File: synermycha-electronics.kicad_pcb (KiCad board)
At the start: 4 copper layers, 128 x 124.5 mm, 114 parts, among them J10 Conn_01x04, J11 USB_B_Micro, J2 Conn_01x02, J3 Conn_01x02, J4 USB_B_Micro, J5 ESP_01, J6 Conn_01x04, J7 Conn_01x04, J8 Conn_01x04, J9 Conn_01x04, Q1 IRLML9301TRPBF, Q2 Q_NPN_EBC, Q3 Q_NPN_EBC, Q4 BC847, SW1 DTSM32N, SW2 DTSM32N, SW3 DTSM32N, SW4 DTSM32N, SW5 SW_SPDT, U1 LM1117LDX, U10 AS5045B, U11 AS5045B, U12 MPU-9250, U13 STM32F446RETx, U14 STM14_SW, U2 LM1117LDX, U3 LM1117LDX, U4 DRV8835, U5 VL53L0X, U6 VL53L0X, U7 VL53L0X, U8 CP2102N-A01-GQFN28, U9 TS5A3167DBVR, Y1 16MHz, 8pF

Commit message: Major upgrade
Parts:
- removed R11, R12, R13: 47K, Resistor_SMD:R_0402_1005Metric
- removed SW5: SW_SPDT, Connector_PinHeader_2.54mm:PinHeader_2x03_P2.54mm_Vertical_SMD
- removed U5, U6, U7: VL53L0X, synermycha-electronics:SENSOR_VL53L0X
- added J1: BATT, Connector_PinHeader_2.54mm:PinHeader_1x02_P2.54mm_Vertical, F.Cu at (38.5, 188.0)
- added J12: Conn_01x05, connector_brd2brd:01x05_1.0x0.5mm_SMD, F.Cu at (37.0, 126.0)
- added J13: Conn_01x05, connector_brd2brd:01x05_1.0x0.5mm_SMD, F.Cu at (59.0, 148.0)
- added J14: Conn_01x05, connector_brd2brd:01x05_1.0x0.5mm_SMD, F.Cu at (15.0, 148.0)
- added J15: Conn_01x05, connector_brd2brd:01x05_1.0x0.5mm_SMD, F.Cu at (21.3, 133.3)
- added J16: Conn_01x05, connector_brd2brd:01x05_1.0x0.5mm_SMD, F.Cu at (52.7, 133.3)
- added J17: Conn_01x03, Button_Switch_SMD:SW_SPDT_CK-JS102011SAQN, F.Cu at (37.0, 194.0)
- BZ1: value SMT-0825-T-2 -> CMT-5023S
- D10, D11, D12, D13, D7, D8, D9: footprint LED_SMD:LED_WS2812B_PLCC4_5.0x5.0mm_P3.2mm -> WS2812-2020:WS28122020
- R21: footprint Resistor_SMD:R_0805_2012Metric -> Resistor_SMD:R_0402_1005Metric
- moved C10 77.4 mm to (88.0, 165.5)
- moved R7 77.4 mm to (89.2, 165.5)
- moved R26 43.5 mm to (28.8, 145.8), turned to 0 degrees
- moved C12 39.8 mm to (91.0, 176.0)
- moved R9 38.0 mm to (91.0, 178.0)
- moved R8 30.0 mm to (80.0, 172.0)
- moved C11 29.8 mm to (80.0, 174.0)
- moved D6 29.3 mm to (24.2, 144.8)
- moved G*** 29.3 mm to (22.0, 147.0)
- moved U14 28.1 mm to (48.0, 144.0), turned to 180 degrees
- moved C21 26.2 mm to (-66.0, 201.7)
- moved C22 26.2 mm to (-66.6, 203.9)
- moved C23 26.2 mm to (-63.6, 203.9)
- moved C20 26.2 mm to (-63.4, 199.2)
- moved J10 26.2 mm to (-70.8, 202.9)
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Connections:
- J7 pad 3: (no net) -> /Encoders/ENC_L_A
- J7 pad 4: (no net) -> /Encoders/ENC_L_B
- J8 pad 3: (no net) -> /Encoders/ENC_R_A
- J8 pad 4: (no net) -> /Encoders/ENC_R_B
- U12 pad 23: (no net) -> /IMU/IMU_SCL
- U12 pad 24: (no net) -> /IMU/IMU_SDA
- U13 pad 16: (no net) -> /WiFi/ESP_RX
- U13 pad 17: (no net) -> /WiFi/ESP_TX
- U13 pad 22: (no net) -> /Encoders/ENC_R_A
- U13 pad 23: (no net) -> /Encoders/ENC_R_B
- U13 pad 33: (no net) -> /Motors & Motors Drivers/DRV8835_EN
- U13 pad 34: (no net) -> /Motors & Motors Drivers/DRV8835_DIR_A
- U13 pad 35: (no net) -> /Motors & Motors Drivers/DRV8835_PWM_A
- U13 pad 36: (no net) -> /Motors & Motors Drivers/DRV8835_PWM_B
- U13 pad 37: (no net) -> /Motors & Motors Drivers/DRV8835_DIR_B
- U13 pad 40: (no net) -> /IMU/IMU_SDA
- U13 pad 41: (no net) -> /IMU/IMU_SCL
- U13 pad 49: (no net) -> /uController/SWDCLK
- U13 pad 55: (no net) -> /uController/SWDO
- U13 pad 58: (no net) -> /Encoders/ENC_L_B
- U13 pad 59: (no net) -> /Encoders/ENC_L_A
- U13 pad 61: (no net) -> /Distance Sensors/VL53L0x_SCL
- U13 pad 62: (no net) -> /Distance Sensors/VL53L0x_SDA
- U14 pad 6: GND -> /uController/SWDCLK
- U14 pad 8: (no net) -> /uController/SWDO
- U4 pad 10: (no net) -> /Motors & Motors Drivers/DRV8835_DIR_A
- U4 pad 11: (no net) -> /Motors & Motors Drivers/DRV8835_EN
- U4 pad 7: (no net) -> /Motors & Motors Drivers/DRV8835_PWM_B
- U4 pad 8: (no net) -> /Motors & Motors Drivers/DRV8835_DIR_B
- U4 pad 9: (no net) -> /Motors & Motors Drivers/DRV8835_PWM_A
- U9 pad 1: (no net) -> /WiFi/ESP_RX
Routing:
- net +2V8: track 18.4 -> 140.6 mm, vias 3 -> 0
- net /Distance Sensors/VL53L0x_SDA: track 0.00 -> 96.4 mm, vias 0 -> 6
- net /Distance Sensors/VL53L0x_SCL: track 0.00 -> 88.3 mm, vias 0 -> 6
- net /uController/STM32_D+: track 0.00 -> 55.3 mm, vias 0 -> 2
- net /uController/STM32_D-: track 0.00 -> 55.3 mm, vias 0 -> 2
- net +6V: track 0.00 -> 42.8 mm
- net +3V3: track 65.8 -> 107.6 mm
- net /Motors & Motors Drivers/DRV8835_PWM_B: track 0.00 -> 21.9 mm, vias 0 -> 2
- net /Motors & Motors Drivers/DRV8835_DIR_B: track 0.00 -> 20.8 mm
- net /Motors & Motors Drivers/DRV8835_PWM_A: track 0.00 -> 20.6 mm
- net /Motors & Motors Drivers/DRV8835_DIR_A: track 0.00 -> 20.2 mm
- net /Motors & Motors Drivers/DRV8835_EN: track 0.00 -> 20.2 mm
- net Net-(Q2-Pad2): track 0.00 -> 16.8 mm
- net /WiFi/ESP_VBUS: track 5.61 -> 18.0 mm
- net /uController/SWDIO: track 0.00 -> 8.93 mm
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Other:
- board size 128 x 124.5 mm -> 50 x 75 mm
- board text added: "+"
- board text added: "-"
- board text added: "2C 7.4V"

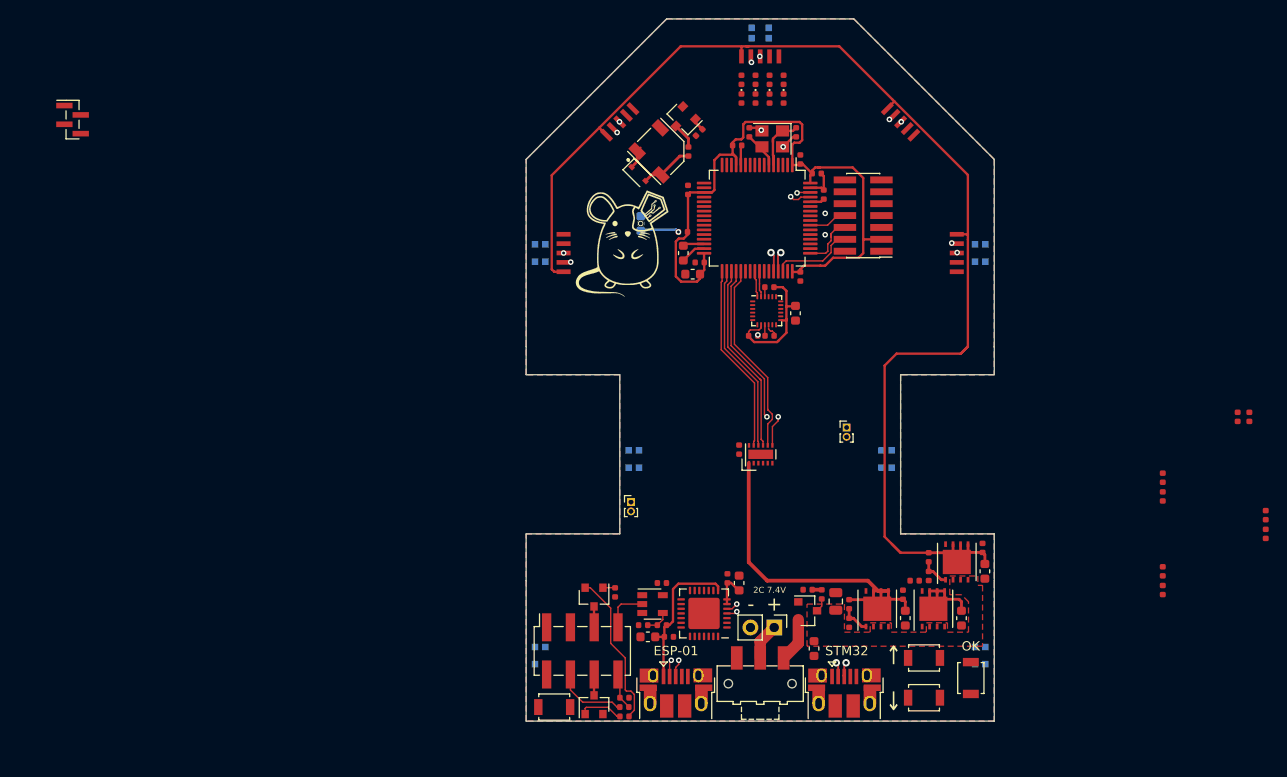
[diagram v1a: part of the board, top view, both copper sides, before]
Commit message: Many updates
Added 3V3<->2V8 conversion for VC53L0x and leds for XSHUT of those. PCB update
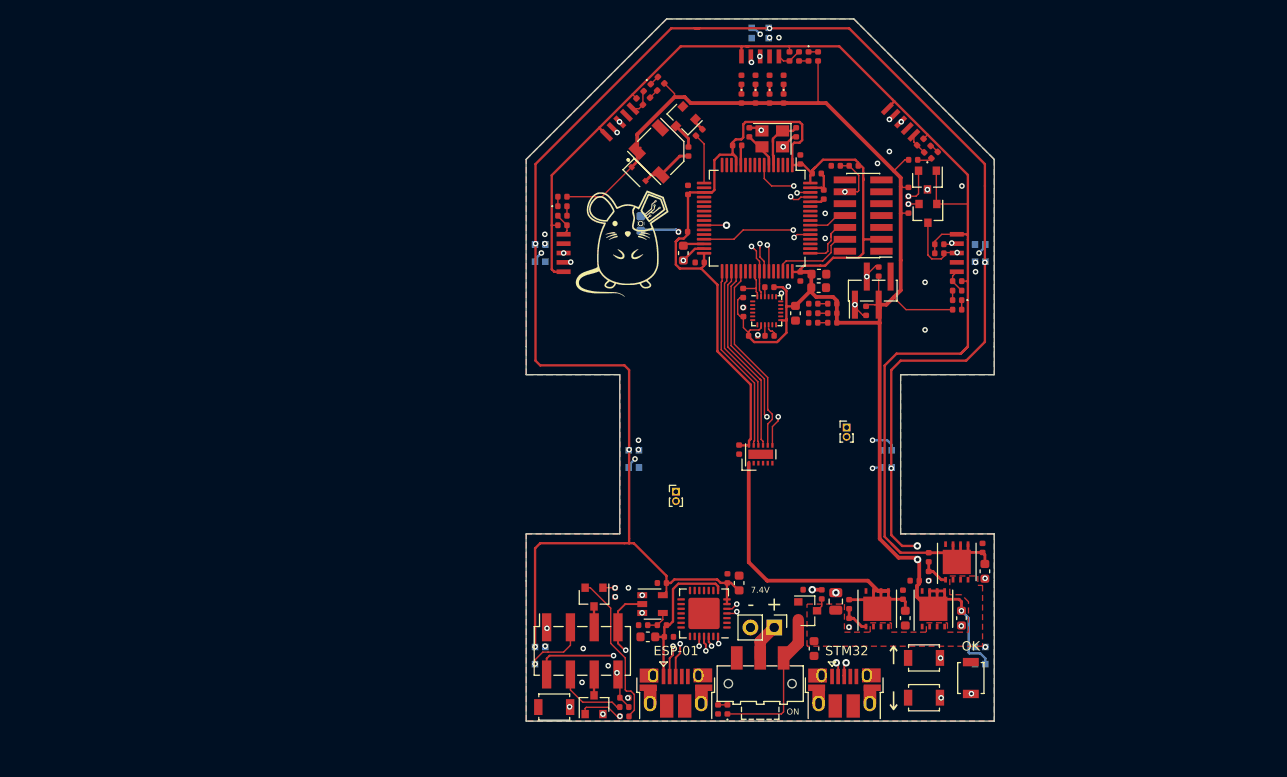
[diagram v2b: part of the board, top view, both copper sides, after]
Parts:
- added C37: 10uF, Capacitor_SMD:C_0603_1608Metric, F.Cu at (43.2, 151.7)
- added D14: RED, LED_SMD:LED_0402_1005Metric, F.Cu at (33.5, 196.8)
- added D15: YELLOW, LED_SMD:LED_0402_1005Metric, F.Cu at (42.2, 127.0)
- added D16: YELLOW, LED_SMD:LED_0402_1005Metric, F.Cu at (58.0, 153.0)
- added D17: YELLOW, LED_SMD:LED_0402_1005Metric, F.Cu at (15.9, 143.0)
- added D18: YELLOW, LED_SMD:LED_0402_1005Metric, F.Cu at (25.7, 130.3)
- added D19: YELLOW, LED_SMD:LED_0402_1005Metric, F.Cu at (55.6, 137.5)
- added Q5: Q_NMOS_GDS, Package_TO_SOT_SMD:SOT-23, F.Cu at (54.9, 140.2)
- added Q6: Q_NMOS_GDS, Package_TO_SOT_SMD:SOT-23, F.Cu at (54.9, 143.8)
- added R11: 2K2, Resistor_SMD:R_0402_1005Metric, F.Cu at (48.3, 154.2)
- added R12: 2K2, Resistor_SMD:R_0402_1005Metric, F.Cu at (35.2, 152.3)
- added R13: 2K2, Resistor_SMD:R_0402_1005Metric, F.Cu at (35.2, 154.3)
- added R30: 2K2, Resistor_SMD:R_0402_1005Metric, F.Cu at (49.7, 150.0)
- added R31: 2K2, Resistor_SMD:R_0402_1005Metric, F.Cu at (52.8, 143.3)
- added R32: 2K2, Resistor_SMD:R_0402_1005Metric, F.Cu at (52.8, 141.5)
- added R33: calculate, Resistor_SMD:R_0402_1005Metric, F.Cu at (32.5, 196.8)
- added R34: 2K2, Resistor_SMD:R_0402_1005Metric, F.Cu at (56.1, 148.0)
- added R35: 2K2, Resistor_SMD:R_0402_1005Metric, F.Cu at (56.1, 147.1)
- added R36: 1K, Resistor_SMD:R_0402_1005Metric, F.Cu at (41.1, 127.0)
- added R37: 1K, Resistor_SMD:R_0402_1005Metric, F.Cu at (58.0, 152.0)
- added R38: 1K, Resistor_SMD:R_0402_1005Metric, F.Cu at (15.9, 144.0)
- added R39: 1K, Resistor_SMD:R_0402_1005Metric, F.Cu at (24.9, 131.1)
- added R40: 1K, Resistor_SMD:R_0402_1005Metric, F.Cu at (54.9, 136.9)
- added R41: 47K, Resistor_SMD:R_0402_1005Metric, F.Cu at (40.1, 127.0)
- added R42: 47K, Resistor_SMD:R_0402_1005Metric, F.Cu at (58.0, 151.0)
- added R43: 47K, Resistor_SMD:R_0402_1005Metric, F.Cu at (15.9, 145.0)
- added R44: 47K, Resistor_SMD:R_0402_1005Metric, F.Cu at (24.1, 131.8)
- added R45: 47K, Resistor_SMD:R_0402_1005Metric, F.Cu at (54.1, 136.1)
- added R46: 1K, Resistor_SMD:R_0402_1005Metric, F.Cu at (43.2, 127.0)
- added R47: 1K, Resistor_SMD:R_0402_1005Metric, F.Cu at (58.0, 154.1)
- added R48: 1K, Resistor_SMD:R_0402_1005Metric, F.Cu at (15.9, 142.0)
- added R49: 1K, Resistor_SMD:R_0402_1005Metric, F.Cu at (26.4, 129.5)
- added R50: 1K, Resistor_SMD:R_0402_1005Metric, F.Cu at (53.3, 138.0)
- J6: footprint Connector_PinHeader_1.00mm:PinHeader_1x04_P1.00mm_Vertical_SMD_Pin1Left -> Connector_PinHeader_1.27mm:PinHeader_1x04_P1.27mm_Vertical_SMD_Pin1Left
- moved J6 87.4 mm to (49.0, 152.0), turned to 90 degrees
- moved C12 53.3 mm to (42.7, 153.4), turned to 180 degrees
- moved R9 52.4 mm to (44.7, 153.4), turned to 180 degrees
- moved C10 50.6 mm to (45.1, 138.7), turned to 180 degrees
- moved R7 50.1 mm to (47.0, 138.7), turned to 180 degrees
- moved C13 47.6 mm to (42.7, 154.4), turned to 180 degrees
- moved R10 44.8 mm to (44.7, 154.4), turned to 180 degrees
- moved C11 41.7 mm to (42.7, 155.4), turned to 180 degrees
- moved R8 39.0 mm to (44.7, 155.4), turned to 180 degrees
- moved C27 13.5 mm to (43.3, 150.3), turned to 180 degrees
- moved J2 4.92 mm to (28.0, 173.5)
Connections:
- J12 pad 1: (no net) -> /Distance Sensors/VL53L0x_~XSHUT[1]
- J13 pad 1: (no net) -> /Distance Sensors/VL53L0x_~XSHUT[2]
- J14 pad 1: (no net) -> /Distance Sensors/VL53L0x_~XSHUT[3]
- J15 pad 1: (no net) -> /Distance Sensors/VL53L0x_~XSHUT[4]
- J16 pad 1: (no net) -> /Distance Sensors/VL53L0x_~XSHUT[5]
- J6 pad 1: (no net) -> /LED & Oled & Buzzer/LCD_SDA
- J6 pad 2: (no net) -> /LED & Oled & Buzzer/LCD_SCL
- R20 pad 2: (no net) -> /LED & Oled & Buzzer/BUZZER
- U13 pad 16: /WiFi/ESP_RX -> (no net)
- U13 pad 17: /WiFi/ESP_TX -> /LED & Oled & Buzzer/BUZZER
- U13 pad 22: /Encoders/ENC_R_A -> /Encoders/ENC_L_B
- U13 pad 23: /Encoders/ENC_R_B -> /Encoders/ENC_L_A
- U13 pad 26: (no net) -> /Power Section/BATT_VOLTAGE
- U13 pad 29: (no net) -> /LED & Oled & Buzzer/LCD_SCL
- U13 pad 42: (no net) -> /WiFi/ESP_RX
- U13 pad 43: (no net) -> /WiFi/ESP_TX
- U13 pad 53: (no net) -> /LED & Oled & Buzzer/LCD_SDA
- U13 pad 58: /Encoders/ENC_L_B -> /Encoders/ENC_R_A
- U13 pad 59: /Encoders/ENC_L_A -> /Encoders/ENC_R_B
- U13 pad 61: /Distance Sensors/VL53L0x_SCL -> Net-(Q5-Pad2)
- U13 pad 62: /Distance Sensors/VL53L0x_SDA -> Net-(Q6-Pad2)
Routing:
- net +3V3: track 107.6 -> 483.9 mm, vias 0 -> 10
- net /WiFi/ESP_TX: track 0.00 -> 72.7 mm, vias 0 -> 3
- net /uController/STM32_D-: track 55.3 -> 1.55 mm, vias 2 -> 1
- net /uController/STM32_D+: track 55.3 -> 1.89 mm, vias 2 -> 1
- net /Power Section/BATT_VOLTAGE: track 1.02 -> 51.2 mm, vias 0 -> 2
- net /WiFi/ESP_RX: track 0.00 -> 49.4 mm, vias 0 -> 2
- net Net-(D10-Pad4): track 0.00 -> 40.5 mm, vias 0 -> 2
- net Net-(D10-Pad2): track 0.00 -> 40.5 mm, vias 0 -> 2
- net Net-(D8-Pad2): track 0.00 -> 32.4 mm, vias 0 -> 2
- net Net-(D11-Pad2): track 0.00 -> 31.5 mm, vias 0 -> 2
- net Net-(D7-Pad2): track 0.00 -> 31.3 mm, vias 0 -> 2
- net Net-(D12-Pad2): track 0.00 -> 30.1 mm, vias 0 -> 2
- net /LED & Oled & Buzzer/LCD_SCL: track 0.00 -> 24.8 mm, vias 0 -> 2
- net /LED & Oled & Buzzer/LCD_SDA: track 0.00 -> 21.2 mm, vias 0 -> 2
- net Net-(Q2-Pad1): track 1.31 -> 21.5 mm, vias 0 -> 2
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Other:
- board text added: "7.4V"
- board text added: "ON"
- board text removed: "2C 7.4V"

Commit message: Adjusted connections, wiring almost finished
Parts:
- added D20: WS2812B, WS2812-2020:WS28122020, B.Cu at (20.5, 131.8)
- added D21: WS2812B, WS2812-2020:WS28122020, B.Cu at (53.8, 132.0)
- added G***: LOGO, synermycha-electronics:Synergia_logo_horizontal_11.4x1.8mm, B.Cu at (46.0, 179.0)
- added G***: LOGO, synermycha-electronics:SynerMycha_napis_silk_screen_45.1x17mm, B.Cu at (38.0, 163.0)
- J6: value Conn_01x04 -> A1250WV-S-4P; footprint Connector_PinHeader_1.27mm:PinHeader_1x04_P1.27mm_Vertical_SMD_Pin1Left -> Connector_JST:JST_GH_BM04B-GHS-TBT_1x04-1MP_P1.25mm_Vertical
- moved J8 143.1 mm to (59.8, 158.5)
- moved J7 85.3 mm to (14.5, 158.5)
- moved R11 5.96 mm to (52.0, 149.5)
- moved J6 2.02 mm to (50.4, 153.5), turned to 180 degrees
- moved R30 1.43 mm to (51.0, 149.5), turned to 270 degrees
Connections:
- D11 pad 4: Net-(D10-Pad2) -> Net-(D11-Pad4)
- D13 pad 2: (no net) -> Net-(D13-Pad2)
- D9 pad 2: Net-(D10-Pad4) -> Net-(D20-Pad4)
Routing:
- net /Buttons/~RESET: track 16.2 -> 95.4 mm, vias 2 -> 4
- net /Buttons/~BUTTON_DOWN: track 1.06 -> 54.0 mm, vias 1 -> 2
- net /Buttons/~BUTTON_OK: track 1.06 -> 48.8 mm, vias 1 -> 2
- net /Buttons/~BUTTON_UP: track 1.07 -> 43.4 mm, vias 1 -> 2
- net Net-(D20-Pad4): track 0.00 -> 20.5 mm, vias 0 -> 2
- net Net-(D11-Pad4): track 0.00 -> 20.3 mm, vias 0 -> 3
- net Net-(D10-Pad4): track 40.5 -> 20.9 mm
- net Net-(D10-Pad2): track 40.5 -> 21.2 mm
- net +3V3: track 483.9 -> 473.8 mm, vias 10 -> 12
- net /LED & Oled & Buzzer/LCD_SDA: track 21.2 -> 19.2 mm
- net GND: vias 30 -> 35
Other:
- board text added: "BY"

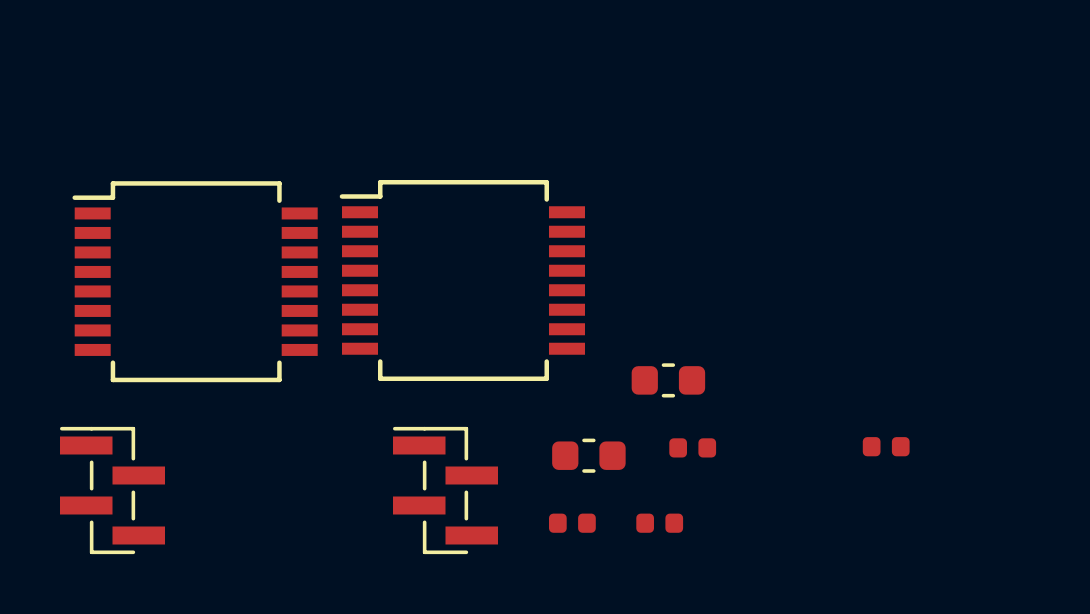
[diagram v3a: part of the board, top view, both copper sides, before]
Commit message: Changes in pcb traces names
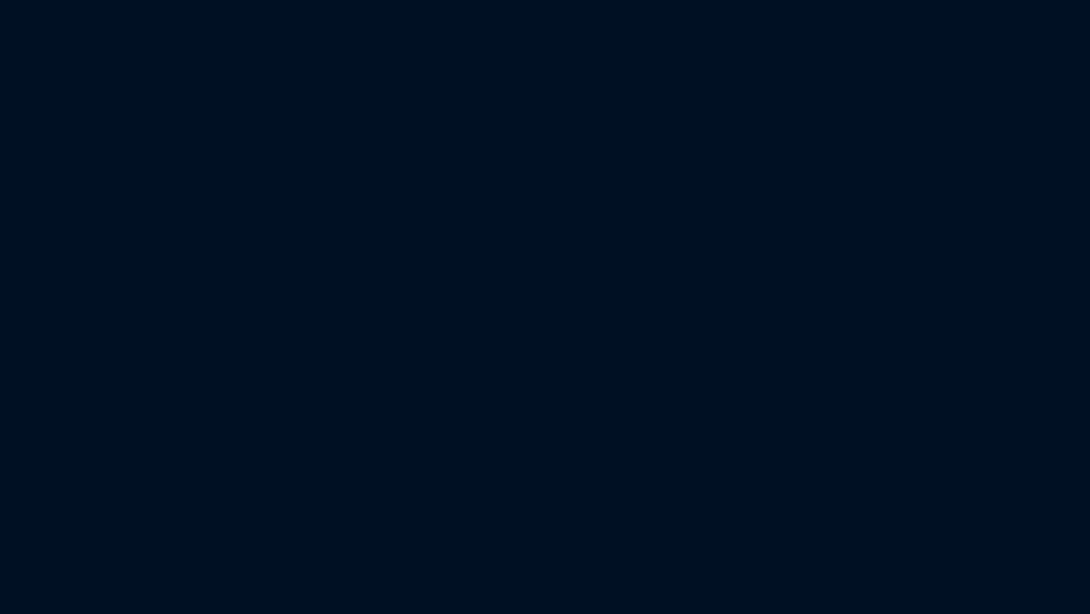
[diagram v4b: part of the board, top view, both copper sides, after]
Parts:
- removed C20, C21: 10uF, Capacitor_SMD:C_0603_1608Metric
- removed C22, C23: 0.1uF, Capacitor_SMD:C_0402_1005Metric
- removed J10, J9: Conn_01x04, Connector_PinHeader_1.00mm:PinHeader_1x04_P1.00mm_Vertical_SMD_Pin1Left
- removed R27, R28: 10K, Resistor_SMD:R_0402_1005Metric
- removed U10, U11: AS5045B, Package_SO:SSOP-16_5.3x6.2mm_P0.65mm
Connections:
- D13 pad 2: Net-(D13-Pad2) -> (no net)
